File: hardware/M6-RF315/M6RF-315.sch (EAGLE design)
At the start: 13 parts, among them J1 CON-71439-2164, M1 MOUNT-HOLE3.3, M2 MOUNT-HOLE3.3, M3 MOUNT-HOLE3.3, M4 MOUNT-HOLE3.3, M5 FIDUCIAL1X2, M6 FIDUCIAL1X2, M7 FIDUCIAL1X2, M8 FIDUCIAL1X2

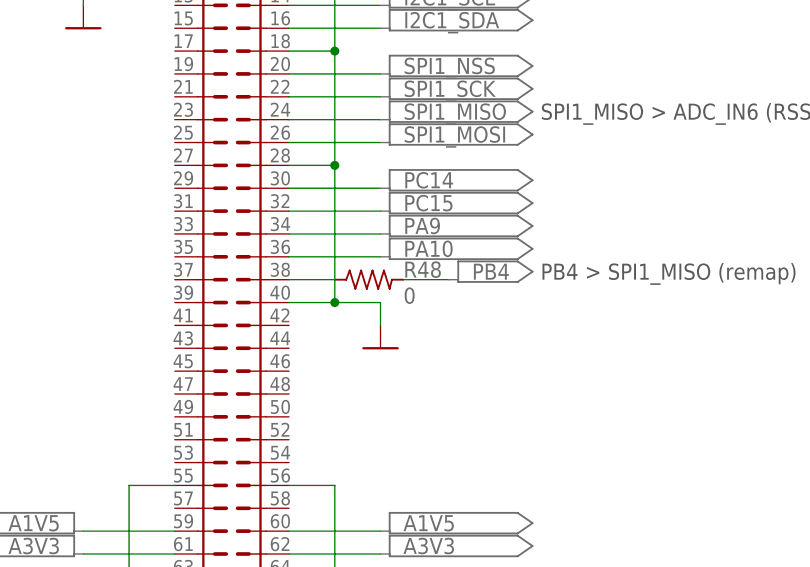
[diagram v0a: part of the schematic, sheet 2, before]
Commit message: 
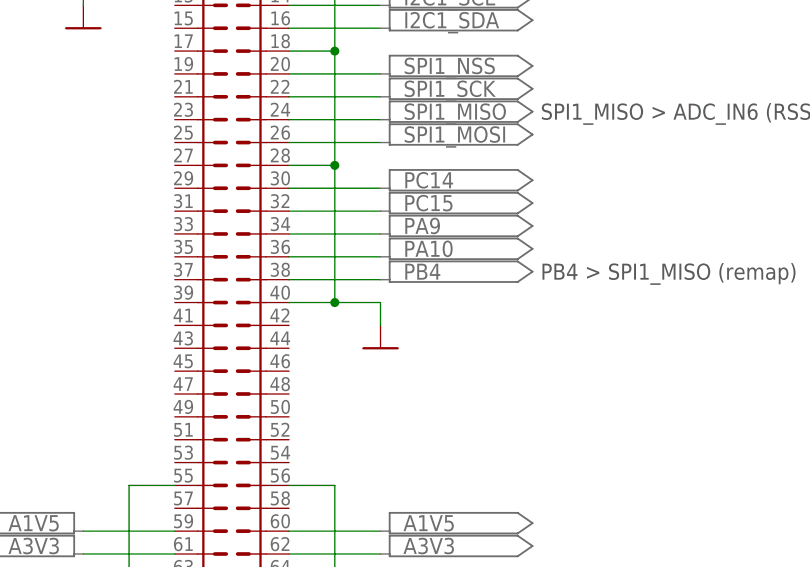
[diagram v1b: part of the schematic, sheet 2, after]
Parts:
- removed R48: 0, powerboard:R0603
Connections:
- removed net PB4-SF: J1.38, R48.1
- net PB4: now also J1.38; no longer R48.2
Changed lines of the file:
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@@
 <part name="PORT99" library="powerboard" deviceset="PORT7" device=""/>
 <part name="PORT100" library="powerboard" deviceset="PORT7" device=""/>
-<part name="PORT101" library="powerboard" deviceset="PORT3" device=""/>
-<part name="R48" library="powerboard" deviceset="R" device="0603" value="0"/>
 <part name="PORT2" library="powerboard" deviceset="PORT7" device=""/>
 <part name="PORT114" library="powerboard" deviceset="PORT7" device=""/>
@@
 <part name="PORT91" library="powerboard" deviceset="PORT7" device=""/>
 <part name="U$4" library="powerboard" deviceset="DGND" device=""/>
+<part name="PORT1" library="powerboard" deviceset="PORT7" device=""/>
 </parts>
 <sheets>
@@
 <instance part="PORT99" gate="G$1" x="88.9" y="104.14"/>
 <instance part="PORT100" gate="G$1" x="88.9" y="101.6"/>
-<instance part="PORT101" gate="G$1" x="88.9" y="96.52"/>
-<instance part="R48" gate="G$1" x="73.66" y="96.52" smashed="yes">
-<attribute name="NAME" x="76.2" y="96.7486" size="1.778" layer="95"/>
-<attribute name="VALUE" x="76.2" y="93.853" size="1.778" layer="96"/>
-</instance>
 <instance part="PORT2" gate="G$1" x="88.9" y="124.46"/>
 <instance part="PORT114" gate="G$1" x="88.9" y="127"/>
@@
 <instance part="PORT91" gate="G$1" x="25.4" y="66.04" rot="MR0"/>
 <instance part="U$4" gate="G$1" x="40.64" y="124.46"/>
+<instance part="PORT1" gate="G$1" x="88.9" y="96.52"/>
 </instances>
 <busses>
@@
 <net name="PB4" class="0">
 <segment>
-<wire x1="76.2" y1="96.52" x2="81.28" y2="96.52" width="0.1524" layer="91"/>
-<label x="83.82" y="96.52" size="1.778" layer="95"/>
-<pinref part="R48" gate="G$1" pin="2"/>
+<label x="76.2" y="96.52" size="1.778" layer="95"/>
+<pinref part="J1" gate="G$1" pin="38"/>
+<wire x1="73.66" y1="96.52" x2="63.5" y2="96.52" width="0.1524" layer="91"/>
 </segment>
 </net>
@@
 </segment>
 </net>
-<net name="PB4-SF" class="0">
-<segment>
-<wire x1="68.58" y1="96.52" x2="63.5" y2="96.52" width="0.1524" layer="91"/>
-<pinref part="R48" gate="G$1" pin="1"/>
-<pinref part="J1" gate="G$1" pin="38"/>
-</segment>
-</net>

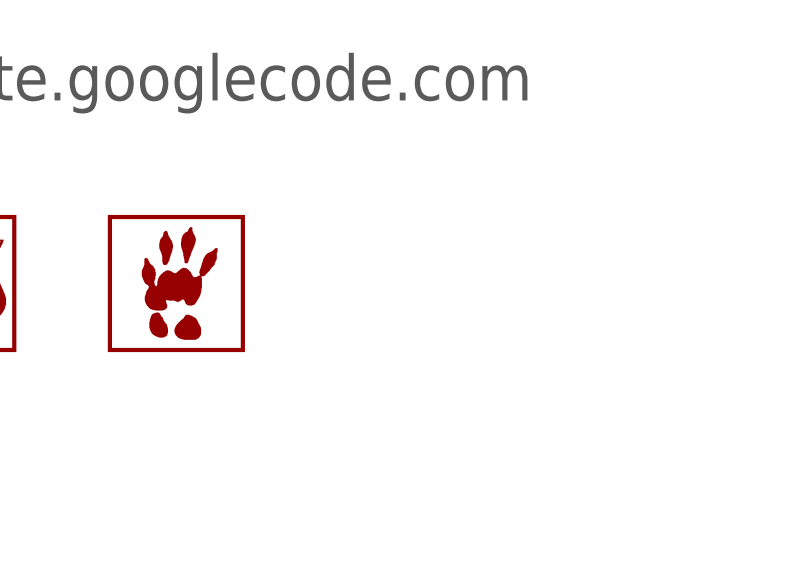
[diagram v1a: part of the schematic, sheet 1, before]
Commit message: Added logo, CC1101 and filled up library with several other components.
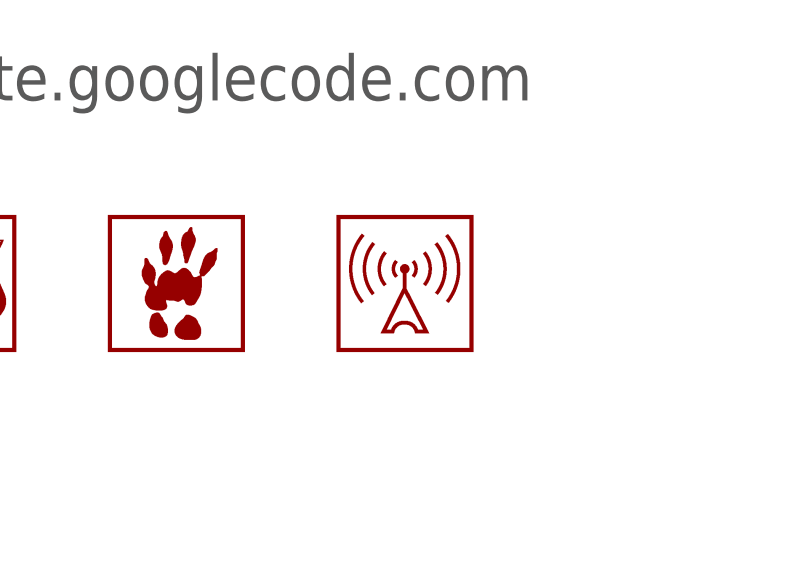
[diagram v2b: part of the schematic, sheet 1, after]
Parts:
- added C1, C2, C3, C4, C5, C6: 100nF, M6-RF315:C0603
- added C7, C8: (no value), M6-RF315:C0603
- added R1: (no value), M6-RF315:R0603
- added R2: 100k, M6-RF315:R0603
- added TP1, TP2: TESTPOINT-RED, M6-RF315:TESTPOINT-RED
- added U$3: LOGO-RADIO-2-600MIL-10MM-AU, M6-RF315:LOGO-RADIO-2-600MIL-10MM-AU
- added U1: CC1101RTKR, M6-RF315:CC1101RTKR
- added X1: CON-SMA, M6-RF315:CON-SMA
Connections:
- new net N$1: J1.34, U1.GDO2
- new net N$2: U1.SO/GDO1
- new net N$3: R1.1, U1.RBIAS
- new net N$4: C6.1, U1.DCOUPL
- new net N$5: C6.2
- new net N$6: C8.1, U1.XOSC_Q2
- new net N$7: C7.1, U1.XOSC_Q1
- net A3V3: now also C1.1, C2.1, C3.1, C4.1, U1.AVDD@2, U1.AVDD@3, U1.AVDD@4, U1.DGUARD
- net AGND: now also C1.2, C2.2, C3.2, C4.2, C7.2, C8.2, R1.2, U1.AGND
- net D3V3: now also C5.1, R2.2, U1.AVDD@1, U1.DVDD
- net DGND: now also C5.2, U1.DGND
- net PA10: now also TP2.1
- net PA9: now also TP1.1, U1.GDO0/ATEST; no longer J1.34
- net SPI1_MOSI: now also U1.SI
- net SPI1_NSS: now also R2.1, U1.CS_N
- net SPI1_SCK: now also U1.SCLK
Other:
- note added: "- Add crystal to library"
- note added: "- Add crystal to schematic"
- note added: "Consider remapping SPI MISO if an ADC is needed"
- note added: "NOTE:"
- note added: "SERIAL RX DATA"
- note added: "SERIAL TX DATA"
- note removed: "- Add SMA connector to library"
- note removed: "- Add logo to library"
- note removed: "- Add transceiver chip to library"
- note removed: "- Select transceiver chip"

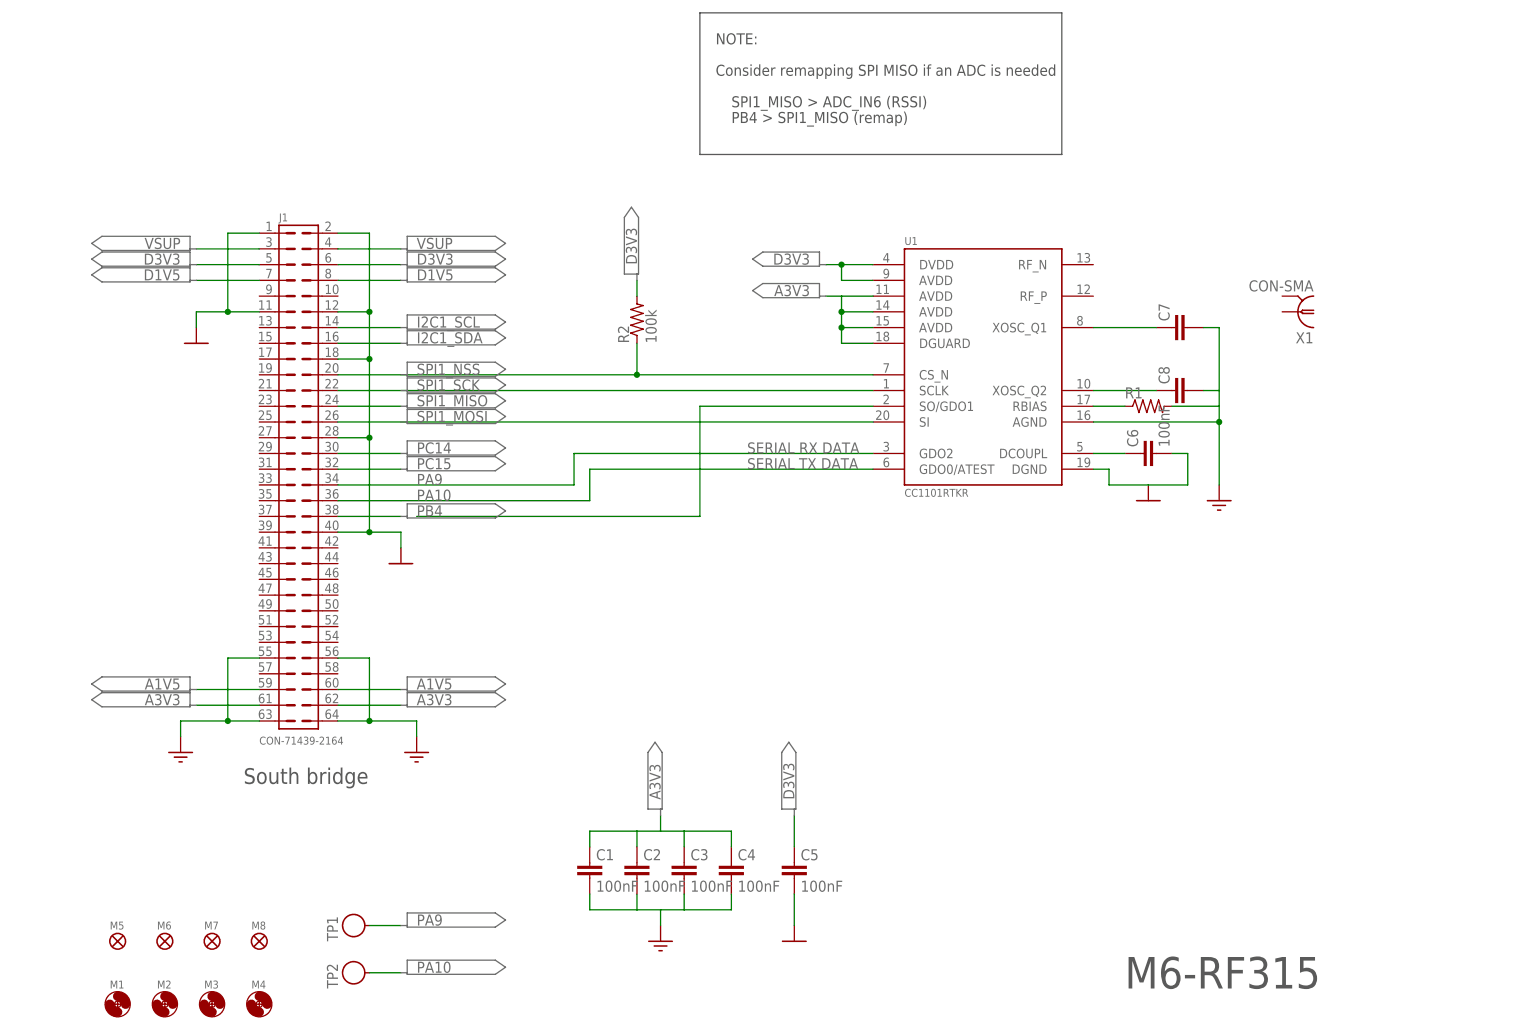
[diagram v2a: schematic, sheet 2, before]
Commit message: All components drawn and added. PCB placed initially.
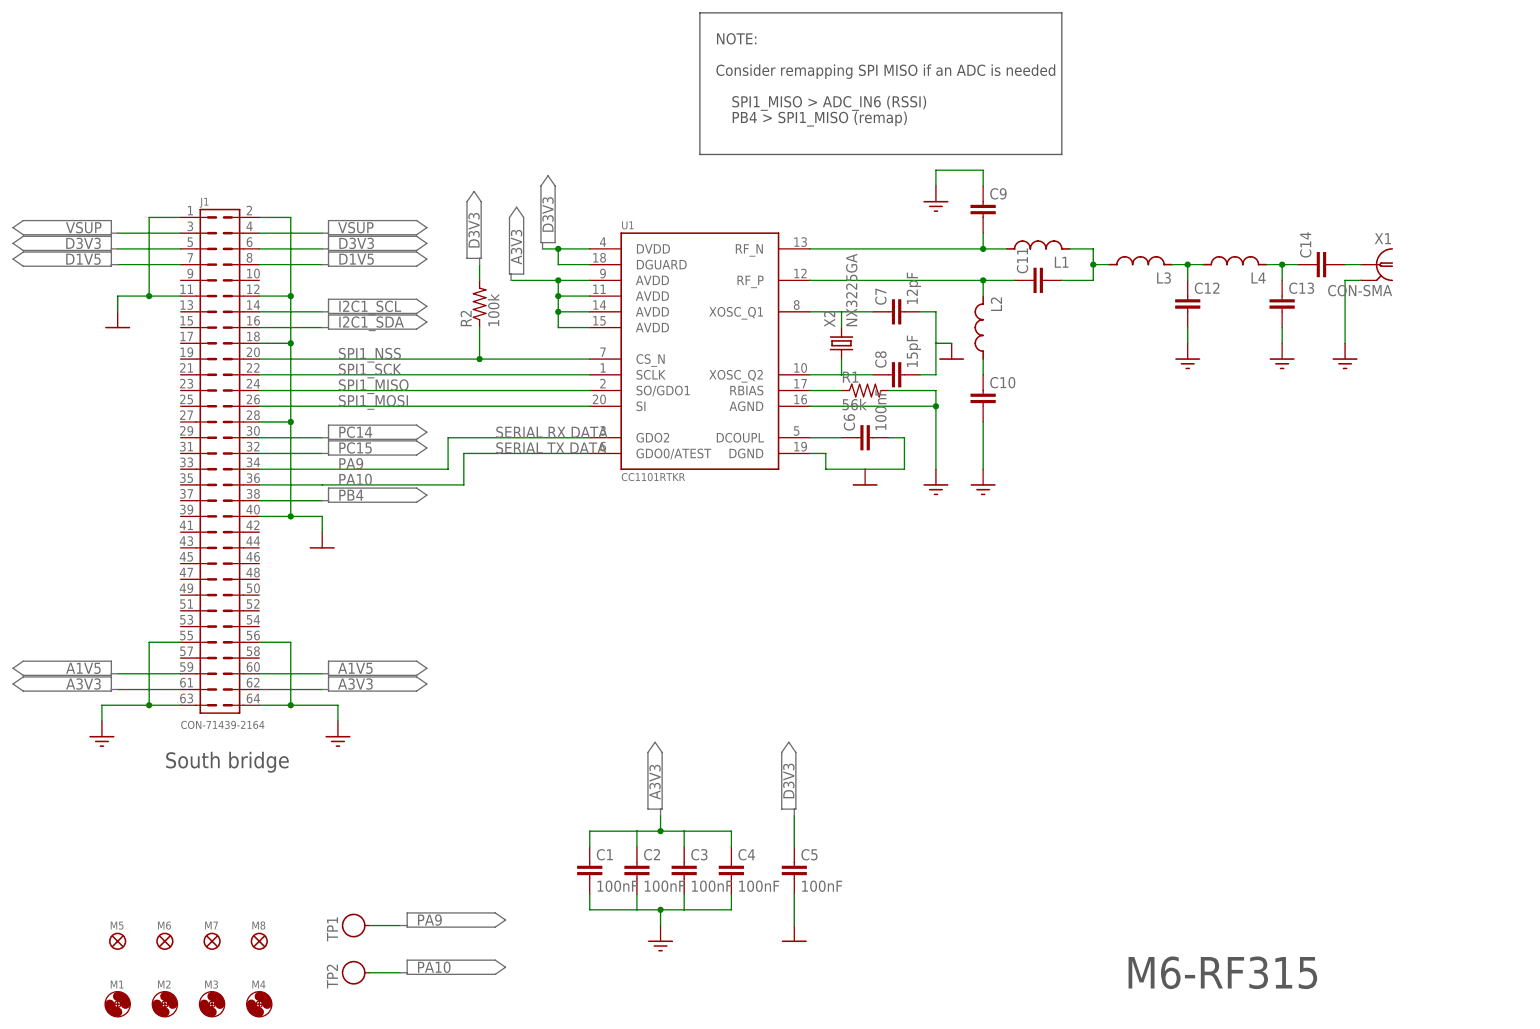
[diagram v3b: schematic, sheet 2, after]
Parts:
- added C10, C11, C12, C13, C14, C9: (no value), M6-RF315:C0603
- added L1, L2, L3, L4: (no value), M6-RF315:L0603
- added X2: NX3225GA, M6-RF315:NX3225GA
- C7: value (none) -> 12pF
- C8: value (none) -> 15pF
- R1: value (none) -> 56k
- U$3: value LOGO-RADIO-2-600MIL-10MM-AU -> LOGO-RADIO-2-600MIL-10MM-CU; device M6-RF315:LOGO-RADIO-2-600MIL-10MM-AU -> M6-RF315:LOGO-RADIO-2-600MIL-10MM-CU
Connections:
- new net N$10: C11.2, L1.2, L3.1
- new net N$11: C13.1, C14.1, L4.2
- new net N$12: C14.2, X1G$1.1
- new net N$13: C10.1, L2.1
- new net N$8: C11.1, L2.2, U1.RF_P
- new net N$9: C9.2, L1.1, U1.RF_N
- net A3V3: now also U1.AVDD@1; no longer U1.DGUARD
- net AGND: now also C10.2, C12.2, C13.2, C9.1, X1G$1.GND; no longer C7.2, C8.2
- net D3V3: now also U1.DGUARD; no longer U1.AVDD@1
- net DGND: now also C7.2, C8.2
- net N$2: now also C12.1, L3.2, L4.1; no longer U1.SO/GDO1
- net N$6: now also X2.1
- net N$7: now also X2.2
- net SPI1_MISO: now also U1.SO/GDO1
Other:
- note added: "- Antenna matching circuit values"
- note added: "- CC1101 PCB layout recommendations (footprint)"
- note added: "- GND planes"
- note added: "- Rbias value"
- note added: "- TX/RX LEDs on I2C/PB4 (optional)"
- note removed: "- Add crystal to library"
- note removed: "- Add crystal to schematic"
- moved on the sheet: C6, C7, C8, J1, R1, R2, U1, X1

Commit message: Antenna part no.
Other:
- note added: "Digikey: ANT-315-CW-RH-SMA-ND"
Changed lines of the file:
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@@
 <?xml version="1.0" encoding="utf-8"?>
 <!DOCTYPE eagle SYSTEM "eagle.dtd">
-<eagle version="6.1">
+<eagle version="6.0">
 <drawing>
 <settings>
@@
 <setting verticaltext="up"/>
 </settings>
-<grid distance="0.1" unitdist="inch" unit="inch" style="lines" multiple="1" display="no" altdistance="0.05" altunitdist="inch" altunit="inch"/>
+<grid distance="0.1" unitdist="inch" unit="inch" style="lines" multiple="1" display="no" altdistance="0.01" altunitdist="inch" altunit="inch"/>
 <layers>
 <layer number="1" name="Top" color="4" fill="1" visible="no" active="no"/>
@@
 <text x="162.56" y="50.8" size="2.54" layer="98">- TX/RX LEDs on I2C/PB4 (optional)</text>
 <text x="162.56" y="45.72" size="2.54" layer="98">- GND planes</text>
+<text x="238.76" y="149.86" size="1.778" layer="98" rot="R270">Digikey: ANT-315-CW-RH-SMA-ND</text>
 </plain>
 <instances>
